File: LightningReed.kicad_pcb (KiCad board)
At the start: 0 parts

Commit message: Complete footprints
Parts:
- added C1: 470nF, LightningReed:C_Rect_L10.0mm_W6.0mm_P7.50mm_MKS4, F.Cu at (67.2, 63.9)
- added C10: 68uF, Capacitor_THT:CP_Radial_D18.0mm_P7.50mm, F.Cu at (25.8, 54.9)
- added C11: 1uF, Capacitor_SMD:C_0603_1608Metric, F.Cu at (21.2, 28.8)
- added C12: 1uF, Capacitor_SMD:C_0603_1608Metric, F.Cu at (21.2, 31.3)
- added C13: 1uF, Capacitor_SMD:C_0603_1608Metric, F.Cu at (21.2, 33.8)
- added C14: 220pF, Capacitor_SMD:C_0603_1608Metric, F.Cu at (21.2, 36.3)
- added C15: 1uF, Capacitor_SMD:C_0603_1608Metric, F.Cu at (21.2, 38.9)
- added C16: 100nF, Capacitor_SMD:C_0805_2012Metric, F.Cu at (84.6, 78.0)
- added C17: 220pF, Capacitor_SMD:C_0603_1608Metric, F.Cu at (21.2, 41.4)
- added C18: 100nF, Capacitor_SMD:C_1206_3216Metric, F.Cu at (55.9, 64.4)
- added C19: 470nF, Capacitor_SMD:C_1812_4532Metric, F.Cu at (39.6, 67.2)
- added C2: 220nF, LightningReed:C_Rect_L10.0mm_W6.0mm_P7.50mm_MKS4, F.Cu at (67.2, 71.5)
- added C20: 330nF, Capacitor_SMD:C_1210_3225Metric, F.Cu at (79.6, 62.3)
- added C21: 330nF, Capacitor_SMD:C_1210_3225Metric, F.Cu at (79.6, 66.5)
- added C22: 330nF, Capacitor_SMD:C_1210_3225Metric, F.Cu at (79.6, 70.8)
- added C23: 47nF, Capacitor_SMD:C_0603_1608Metric, F.Cu at (21.2, 43.9)
- added C24: 100nF, Capacitor_SMD:C_0603_1608Metric, F.Cu at (25.2, 16.3)
- added C25: 1uF, Capacitor_SMD:C_0603_1608Metric, F.Cu at (25.2, 18.8)
- added C26: 2.2uF, Capacitor_SMD:C_0603_1608Metric, F.Cu at (25.2, 21.3)
- added C27: 4.7uF, Capacitor_SMD:C_1210_3225Metric, F.Cu at (79.6, 75.0)
- added C28: 4.7uF, Capacitor_SMD:C_0805_2012Metric, F.Cu at (84.6, 81.0)
- added C29: 22uF, Capacitor_SMD:C_1210_3225Metric, F.Cu at (79.6, 79.3)
- added C30: 100nF, Capacitor_SMD:C_0603_1608Metric, F.Cu at (25.2, 23.8)
- added C31: 220pF, Capacitor_SMD:C_0603_1608Metric, F.Cu at (25.2, 26.3)
- added C32: 220pF, Capacitor_SMD:C_0603_1608Metric, F.Cu at (25.2, 28.8)
- added C33: 33pF, Capacitor_SMD:C_0603_1608Metric, F.Cu at (25.2, 31.3)
- added C34: 22pF, Capacitor_SMD:C_0603_1608Metric, F.Cu at (25.2, 33.8)
- added C35: 4.7nF, Capacitor_SMD:C_0603_1608Metric, F.Cu at (25.2, 36.3)
- added C36: 10nF, Capacitor_SMD:C_0603_1608Metric, F.Cu at (25.2, 38.9)
- added C37: 3.3pF, Capacitor_SMD:C_0603_1608Metric, F.Cu at (25.2, 41.4)
- added C38: 220pF, Capacitor_SMD:C_0603_1608Metric, F.Cu at (25.2, 43.9)
- added C39: 33uF, Capacitor_SMD:C_1206_3216Metric, F.Cu at (55.9, 67.7)
- added C4: 10pF, Capacitor_SMD:C_0805_2012Metric, F.Cu at (84.6, 75.0)
- added C40: 33uF, Capacitor_SMD:C_1206_3216Metric, F.Cu at (55.9, 71.1)
- added C41: 33uF, Capacitor_SMD:C_1206_3216Metric, F.Cu at (55.9, 74.4)
- added C42: 33uF, Capacitor_SMD:C_1206_3216Metric, F.Cu at (55.9, 77.8)
- added C43: 680uF, Capacitor_SMD:CP_Elec_10x10, F.Cu at (75.2, 38.3)
- added C44: 1uF, Capacitor_SMD:C_0603_1608Metric, F.Cu at (29.3, 16.3)
- added C45: 1uF, Capacitor_SMD:C_0603_1608Metric, F.Cu at (29.3, 18.8)
- added C46: 1uF, Capacitor_SMD:C_0603_1608Metric, F.Cu at (29.3, 21.3)
- added C47: 2.2uF, Capacitor_SMD:C_0603_1608Metric, F.Cu at (29.3, 23.8)
- added C5: 3900pF, Capacitor_SMD:C_0603_1608Metric, F.Cu at (21.2, 16.3)
- added C6: 1uF, Capacitor_SMD:C_0603_1608Metric, F.Cu at (21.2, 18.8)
- added C7: 33nF, Capacitor_SMD:C_0603_1608Metric, F.Cu at (21.2, 21.3)
- added C8: 220pF, Capacitor_SMD:C_0603_1608Metric, F.Cu at (21.2, 23.8)
- added C9: 2200pF, Capacitor_SMD:C_0603_1608Metric, F.Cu at (21.2, 26.3)
- added D1: ES3JF, Diode_SMD:D_SMF, F.Cu at (61.6, 64.4)
- added D10: SD103AW, Diode_SMD:D_SOD-123, F.Cu at (61.6, 71.1)
- added D11: BAS70WS, Diode_SMD:D_SOD-323, F.Cu at (45.4, 59.0)
- added D12: BZX84C16, Package_TO_SOT_SMD:SOT-23, F.Cu at (45.7, 34.6)
- added D13: MM3Z20, Diode_SMD:D_SOD-323, F.Cu at (45.4, 62.0)
- added D14: MM3Z24, Diode_SMD:D_SOD-323, F.Cu at (45.4, 64.9)
- added D15: RF081M2STR, Diode_SMD:D_SOD-123, F.Cu at (61.6, 74.4)
- added D16: MM3Z10, Diode_SMD:D_SOD-323, F.Cu at (45.4, 67.9)
- added D17: RFU02VSM8S, Diode_SMD:D_SOD-523, F.Cu at (80.5, 56.9)
- added D2: MSB40M, LightningReed:UMSB, F.Cu at (71.0, 79.2)
- added D3: ES2JW, Diode_SMD:D_SOD-123F, F.Cu at (84.7, 34.0)
- added D4: BZT52C16S, Diode_SMD:D_SOD-323, F.Cu at (45.4, 56.1)
- added D5: DSK16, Diode_SMD:D_SOD-123F, F.Cu at (84.7, 37.4)
- added D6: BZT52C13, Diode_SMD:D_SOD-123, F.Cu at (61.6, 67.7)
- added D7: STTH1R06A, Diode_SMD:D_SMA, F.Cu at (82.8, 48.9)
- added D8: ES1JW, Diode_SMD:D_SOD-123F, F.Cu at (84.7, 40.7)
- added D9: ES1JW, Diode_SMD:D_SOD-123F, F.Cu at (84.7, 44.1)
- added F1: JFC2410-1500TS, LightningReed:JFC2410, F.Cu at (82.8, 51.9)
- added L1: 5mH, LightningReed:CHOKE, F.Cu at (44.1, 15.8)
- added L2: 5mH, LightningReed:CHOKE, F.Cu at (44.1, 24.5)
- added L3: SDA0912-150uH-0.45, Inductor_THT:L_Radial_D12.0mm_P5.00mm_Fastron_11P, F.Cu at (69.5, 53.4)
- added L4: 7447709471, Inductor_SMD:L_12x12mm_H8mm, F.Cu at (60.5, 39.5)
- added L5: 1uH, LightningReed:CKST0603, F.Cu at (79.6, 19.1)
- added L6: 680nH, Inductor_SMD:L_0805_2012Metric, F.Cu at (38.3, 81.1)
- added P1: Conn_WallPlug, Connector_Wire:SolderWire-1sqmm_1x02_P5.4mm_D1.4mm_OD2.7mm, F.Cu at (62.5, 29.8)
- added Q1: NCE65T180D, Package_TO_SOT_SMD:TO-263-2, F.Cu at (68.7, 21.2)
- added Q10: DMZ6005E, Package_TO_SOT_SMD:SOT-23, F.Cu at (50.6, 39.0)
- added Q11: 2N7002K, Package_TO_SOT_SMD:SOT-23, F.Cu at (50.6, 43.5)
- added Q12: NCEP15T14D, Package_TO_SOT_SMD:LFPAK33, F.Cu at (38.8, 77.3)
- added Q13: BSS123, Package_TO_SOT_SMD:SOT-23, F.Cu at (50.6, 47.9)
- added Q2: 2N7002, Package_TO_SOT_SMD:SOT-23, F.Cu at (45.7, 39.0)
- added Q4: 2N7002, Package_TO_SOT_SMD:SOT-23, F.Cu at (45.7, 43.5)
- added Q5: 2N7002K, Package_TO_SOT_SMD:SOT-23, F.Cu at (45.7, 47.9)
- added Q6: 2N7002K, Package_TO_SOT_SMD:SOT-23, F.Cu at (45.7, 52.4)
- added Q7: NCE65T260K, Package_TO_SOT_SMD:TO-252-2, F.Cu at (59.1, 50.6)
- added Q8: NCE65T260K, Package_TO_SOT_SMD:TO-252-2, F.Cu at (59.1, 58.7)
- added Q9: NCE0102, Package_TO_SOT_SMD:SOT-23, F.Cu at (50.6, 34.6)
- added R1: 10, Resistor_SMD:R_0603_1608Metric, F.Cu at (29.3, 26.3)
- added R10: 3M24, Resistor_SMD:R_1206_3216Metric, F.Cu at (22.0, 82.8)
- added R11: 3M24, Resistor_SMD:R_1206_3216Metric, F.Cu at (27.6, 66.3)
- added R12: 3M24, Resistor_SMD:R_1206_3216Metric, F.Cu at (27.6, 69.6)
- added R13: 274K, Resistor_SMD:R_0603_1608Metric, F.Cu at (29.3, 36.3)
- added R14: 64k9, Resistor_SMD:R_0603_1608Metric, F.Cu at (29.3, 38.9)
- added R15: 2, Resistor_SMD:R_0603_1608Metric, F.Cu at (29.3, 41.4)
- added R16: 100K, Resistor_SMD:R_0603_1608Metric, F.Cu at (29.3, 43.9)
- added R17: 39K2, Resistor_SMD:R_0603_1608Metric, F.Cu at (33.3, 16.3)
- added R18: 100K, Resistor_SMD:R_0603_1608Metric, F.Cu at (33.3, 18.8)
- added R19: 3M24, Resistor_SMD:R_1206_3216Metric, F.Cu at (27.6, 72.9)
- added R2: 3M24, Resistor_SMD:R_1206_3216Metric, F.Cu at (22.0, 66.3)
- added R20: 3M24, Resistor_SMD:R_1206_3216Metric, F.Cu at (27.6, 76.2)
- added R21: 1K, Resistor_SMD:R_1206_3216Metric, F.Cu at (27.6, 79.5)
- added R22: 1K, Resistor_SMD:R_1206_3216Metric, F.Cu at (27.6, 82.8)
- added R23: 1K, Resistor_SMD:R_1206_3216Metric, F.Cu at (33.3, 66.3)
- added R24: 3M24, Resistor_SMD:R_1206_3216Metric, F.Cu at (33.3, 69.6)
- added R25: 3M16, Resistor_SMD:R_0805_2012Metric, F.Cu at (49.7, 56.1)
- added R26: 178K, Resistor_SMD:R_0603_1608Metric, F.Cu at (33.3, 21.3)
- added R27: 49K9, Resistor_SMD:R_0603_1608Metric, F.Cu at (33.3, 23.8)
- added R28: 100K, Resistor_SMD:R_0603_1608Metric, F.Cu at (33.3, 26.3)
- added R29: 10K, Resistor_SMD:R_0603_1608Metric, F.Cu at (33.3, 28.8)
- added R3: 3M24, Resistor_SMD:R_1206_3216Metric, F.Cu at (22.0, 69.6)
- added R30: 2M21, Resistor_SMD:R_1206_3216Metric, F.Cu at (33.3, 72.9)
- added R31: 10, Resistor_SMD:R_0603_1608Metric, F.Cu at (33.3, 31.3)
- added R32: 10K, Resistor_SMD:R_0603_1608Metric, F.Cu at (33.3, 33.8)
- added R33: 24.9, Resistor_SMD:R_0603_1608Metric, F.Cu at (33.3, 36.3)
- added R34: 10K, Resistor_SMD:R_0603_1608Metric, F.Cu at (33.3, 38.9)
- added R35: 10, Resistor_SMD:R_0603_1608Metric, F.Cu at (33.3, 41.4)
- added R36: 44K2, Resistor_SMD:R_0603_1608Metric, F.Cu at (33.3, 43.9)
- added R37: 118K, Resistor_SMD:R_0603_1608Metric, F.Cu at (37.3, 16.3)
- added R38: 220m, Resistor_SMD:R_1206_3216Metric, F.Cu at (33.3, 76.2)
- added R39: 220m, Resistor_SMD:R_1206_3216Metric, F.Cu at (33.3, 79.5)
- added R4: 3M24, Resistor_SMD:R_1206_3216Metric, F.Cu at (22.0, 72.9)
- added R40: 1, Resistor_SMD:R_0805_2012Metric, F.Cu at (49.7, 59.0)
- added R41: 1, Resistor_SMD:R_0805_2012Metric, F.Cu at (49.7, 62.0)
- added R42: 150K, Resistor_SMD:R_0603_1608Metric, F.Cu at (37.3, 18.8)
- added R43: 150K, Resistor_SMD:R_0603_1608Metric, F.Cu at (37.3, 21.3)
- added R44: 274K, Resistor_SMD:R_0603_1608Metric, F.Cu at (37.3, 23.8)
- added R45: 332K, Resistor_SMD:R_0603_1608Metric, F.Cu at (37.3, 26.3)
- added R46: 332K, Resistor_SMD:R_0603_1608Metric, F.Cu at (37.3, 28.8)
- added R47: 1K21, Resistor_SMD:R_0603_1608Metric, F.Cu at (37.3, 31.3)
- added R48: 1M, Resistor_SMD:R_0603_1608Metric, F.Cu at (37.3, 33.8)
- added R49: 121, Resistor_SMD:R_0603_1608Metric, F.Cu at (37.3, 36.3)
- added R5: 24K3, Resistor_SMD:R_0603_1608Metric, F.Cu at (29.3, 28.8)
- added R50: 12K4, Resistor_SMD:R_0603_1608Metric, F.Cu at (37.3, 38.9)
- added R51: 75K, Resistor_SMD:R_0603_1608Metric, F.Cu at (37.3, 41.4)
- added R52: 30K1, Resistor_SMD:R_0603_1608Metric, F.Cu at (37.3, 43.9)
- added R53: 432K, Resistor_SMD:R_0603_1608Metric, F.Cu at (41.3, 16.3)
- added R54: 10, Resistor_SMD:R_0603_1608Metric, F.Cu at (41.3, 18.8)
- added R55: 562, Resistor_SMD:R_0603_1608Metric, F.Cu at (41.3, 21.3)
- added R56: 10K, Resistor_SMD:R_0603_1608Metric, F.Cu at (41.3, 23.8)
- added R57: 15K, Resistor_SMD:R_0603_1608Metric, F.Cu at (41.3, 26.3)
- added R58: 150K, Resistor_SMD:R_0603_1608Metric, F.Cu at (41.3, 28.8)
- added R59: 56K2, Resistor_SMD:R_0603_1608Metric, F.Cu at (41.3, 31.3)
- added R6: 220m, Resistor_SMD:R_1206_3216Metric, F.Cu at (22.0, 76.2)
- added R60: 150K, Resistor_SMD:R_0603_1608Metric, F.Cu at (41.3, 33.8)
- added R61: 22, Resistor_SMD:R_0805_2012Metric, F.Cu at (49.7, 64.9)
- added R62: 100, Resistor_SMD:R_0603_1608Metric, F.Cu at (41.3, 36.3)
- added R63: 75K, Resistor_SMD:R_0603_1608Metric, F.Cu at (41.3, 38.9)
- added R7: 220m, Resistor_SMD:R_1206_3216Metric, F.Cu at (22.0, 79.5)
- added R8: 182K, Resistor_SMD:R_0603_1608Metric, F.Cu at (29.3, 31.3)
- added R9: 750, Resistor_SMD:R_0603_1608Metric, F.Cu at (29.3, 33.8)
- added TH1: 100K, Resistor_SMD:R_0603_1608Metric, F.Cu at (41.3, 41.4)
- added U1: UCC28056, Package_TO_SOT_SMD:SOT-23-6, F.Cu at (85.0, 62.4)
- added U2: 78L05S, Package_TO_SOT_SMD:SOT-89-3, F.Cu at (61.8, 79.1)
- added U3: LMC7111, Package_TO_SOT_SMD:SOT-23-5, F.Cu at (85.0, 66.8)
- added U4: UCC28780, Package_DFN_QFN:QFN-16-1EP_3x3mm_P0.5mm_EP1.45x1.45mm, F.Cu at (38.7, 72.3)
- added U5: UCC27712, Package_SO:SO-8_3.9x4.9mm_P1.27mm, F.Cu at (47.5, 72.6)
- added U6: LM317G, Package_TO_SOT_SMD:SOT-223-3_TabPin2, F.Cu at (82.4, 27.3)
- added U7: FODM8801A, Package_SO:SOP-4_4.4x2.6mm_P1.27mm, F.Cu at (48.1, 77.9)
- added U8: TL431DBZ, Package_TO_SOT_SMD:SOT-23, F.Cu at (50.6, 52.4)
- added U9: UCC24612-1DBV, Package_TO_SOT_SMD:SOT-23-5, F.Cu at (85.0, 71.3)
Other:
- copper layers 0 -> 2

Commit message: routing 1/?
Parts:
- added C3: 470nF, Capacitor_SMD:C_1812_4532Metric, F.Cu at (109.7, 134.9)
- added Q3: 1N60G, Package_TO_SOT_SMD:SOT-223-3_TabPin2, F.Cu at (35.3, 50.3)
- added T1: Transformer_2P_2S, LightningReed:RM10, F.Cu at (149.4, 126.0)
- added TP1: TestPoint_Alt, Connector_Wire:SolderWire-0.5sqmm_1x01_D0.9mm_OD2.1mm, F.Cu at (38.4, 64.8)
- added TP2: TestPoint_Alt, Connector_Wire:SolderWire-0.5sqmm_1x01_D0.9mm_OD2.1mm, F.Cu at (38.4, 68.9)
- added TP3: TestPoint_Alt, Connector_Wire:SolderWire-0.5sqmm_1x01_D0.9mm_OD2.1mm, F.Cu at (38.4, 73.1)
- added TP4: TestPoint_Alt, Connector_Wire:SolderWire-0.5sqmm_1x01_D0.9mm_OD2.1mm, F.Cu at (38.4, 77.2)
- D2, F1: moved to B.Cu
- Q12: footprint Package_TO_SOT_SMD:LFPAK33 -> Package_TO_SOT_SMD:TO-263-2
- moved L4 119.0 mm to (119.6, 142.7), turned to -90 degrees
- moved L2 110.0 mm to (100.5, 118.9)
- moved L1 105.0 mm to (100.3, 104.5)
- moved L3 96.5 mm to (103.9, 143.5)
- moved P1 83.5 mm to (104.2, 102.1)
- moved D1 81.2 mm to (94.1, 138.8)
- moved C19 77.5 mm to (102.4, 21.7)
- moved Q12 77.3 mm to (90.0, 19.5)
- moved C2 73.4 mm to (103.4, 135.3), turned to 90 degrees
- moved L5 66.6 mm to (42.7, 74.6)
- moved L6 64.4 mm to (102.6, 76.1)
- moved U4 64.2 mm to (103.0, 72.1)
- moved C1 61.8 mm to (101.7, 115.3)
- moved U1 61.4 mm to (101.4, 3.19)
- moved U3 61.4 mm to (101.4, 7.64)
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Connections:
- D12 pad 1: Net-(D12-K) -> GNDPWR
- D12 pad 2: GNDPWR -> (no net)
- D12 pad 3: (no net) -> Net-(D12-K)
- L2 pad 1: Net-(D2-Pad4) -> Net-(C1-Pad1)
- L2 pad 2: Net-(C1-Pad1) -> Net-(D2-Pad4)
- L2 pad 3: Net-(D2-Pad3) -> Net-(C1-Pad2)
- L2 pad 4: Net-(C1-Pad2) -> Net-(D2-Pad3)
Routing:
- net Net-(F1-Pad2): vias 0 -> 18
- net Net-(D2-Pad3): vias 0 -> 12
- net HT: vias 0 -> 12
- added copper zone on B.Cu, net GNDPWR
- added copper zone on F.Cu, net HT
- added copper zone on B.Cu, net Net-(C1-Pad1)
- added copper zone on B.Cu, net Net-(C1-Pad2)
- added copper zone on F.Cu, net Net-(D2-Pad3)
- added copper zone on B.Cu, net Net-(D2-Pad4)
- added copper zone on F.Cu, net Net-(F1-Pad2)
- added copper zone on F.Cu, net Net-(P1-AC_N)
- added copper zone on B.Cu, net Net-(P1-AC_P)
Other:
- board outline added: 50 x 50 mm

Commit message: PFC Layout
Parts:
- C11, C17, C4, C5, C6, C7, C8, D1, D3, D6, Q1, Q5, Q6, R1, R15, R2, R27, R28, R29, R3, R4, R5, R6, R7, R8, R9, U1: moved to B.Cu
- moved C6 180.9 mm to (141.5, 149.1), turned to 180 degrees
- moved C7 177.7 mm to (141.5, 147.6), turned to 180 degrees
- moved C5 171.7 mm to (132.8, 141.5), turned to 180 degrees
- moved C8 170.1 mm to (139.7, 141.7)
- moved C9 168.7 mm to (131.8, 148.6)
- moved R8 166.9 mm to (143.8, 148.3), turned to -90 degrees
- moved R29 164.6 mm to (148.1, 142.7)
- moved R28 164.0 mm to (144.0, 142.5)
- moved C17 163.3 mm to (146.3, 144.3)
- moved R27 162.6 mm to (146.6, 136.3), turned to 90 degrees
- moved C11 160.8 mm to (138.7, 135.4), turned to 90 degrees
- moved R5 158.8 mm to (134.1, 143.0)
- moved R9 157.5 mm to (136.7, 144.5), turned to -90 degrees
- moved R13 154.1 mm to (128.8, 148.6), turned to 180 degrees
- moved R1 152.9 mm to (128.5, 137.2)
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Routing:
- net /VCC_PFC: track 0.00 -> 9.27 mm, vias 0 -> 1
- net VDC: vias 0 -> 18
- net Net-(D3-A): vias 0 -> 30
- net Net-(D1-A): vias 0 -> 4
- net GNDPWR: vias 0 -> 12
- added copper zone on F.Cu, net Net-(D1-A)
- added copper zone on B.Cu, net Net-(D3-A)
- added copper zone on B.Cu, net VDC
- added copper zone on F.Cu, net VDC
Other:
- board size 50 x 50 mm -> 55 x 50 mm

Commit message: SR layout
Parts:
- added REF**: SolderWire-1sqmm_1x01_D1.4mm_OD2.7mm, Connector_Wire:SolderWire-1sqmm_1x01_D1.4mm_OD2.7mm, F.Cu at (127.3, 77.0)
- added TP10: TestPoint, Connector_Wire:SolderWire-0.15sqmm_1x01_D0.5mm_OD1.5mm, F.Cu at (130.6, 101.3)
- added TP11: TestPoint, Connector_Wire:SolderWire-0.15sqmm_1x01_D0.5mm_OD1.5mm, F.Cu at (130.6, 98.6)
- added TP12: TestPoint, Connector_Wire:SolderWire-0.15sqmm_1x01_D0.5mm_OD1.5mm, F.Cu at (127.3, 98.6)
- added TP13: TestPoint, Connector_Wire:SolderWire-0.15sqmm_1x01_D0.5mm_OD1.5mm, F.Cu at (144.3, 101.3)
- added TP14: TestPoint, Connector_Wire:SolderWire-0.15sqmm_1x01_D0.5mm_OD1.5mm, F.Cu at (147.6, 101.3)
- added TP15: TestPoint, Connector_Wire:SolderWire-0.15sqmm_1x01_D0.5mm_OD1.5mm, F.Cu at (144.3, 98.6)
- added TP16: TestPoint, Connector_Wire:SolderWire-0.15sqmm_1x01_D0.5mm_OD1.5mm, F.Cu at (147.6, 98.6)
- added TP5: TestPoint, Connector_Wire:SolderWire-1sqmm_1x01_D1.4mm_OD2.7mm, F.Cu at (140.0, 98.0)
- added TP6: TestPoint, Connector_Wire:SolderWire-1sqmm_1x01_D1.4mm_OD2.7mm, F.Cu at (140.0, 101.9)
- added TP7: TestPoint, Connector_Wire:SolderWire-1sqmm_1x01_D1.4mm_OD2.7mm, F.Cu at (134.6, 98.0)
- added TP8: TestPoint, Connector_Wire:SolderWire-1sqmm_1x01_D1.4mm_OD2.7mm, F.Cu at (134.6, 101.9)
- added TP9: TestPoint, Connector_Wire:SolderWire-0.15sqmm_1x01_D0.5mm_OD1.5mm, F.Cu at (127.3, 101.3)
- C36, C38, C39, C40, C41, C45, C47, D17, L5, L6, R59, R60, R61, R62, U7, U8, U9: moved to B.Cu
- TP1: footprint Connector_Wire:SolderWire-0.5sqmm_1x01_D0.9mm_OD2.1mm -> Connector_Wire:SolderWire-1sqmm_1x01_D1.4mm_OD2.7mm
- moved R24 106.1 mm to (74.9, 128.5)
- moved D4 100.7 mm to (88.7, 123.4)
- moved C36 100.6 mm to (152.1, 87.9)
- moved C35 98.4 mm to (145.5, 91.9), turned to 180 degrees
- moved C37 98.3 mm to (148.6, 91.9)
- moved R57 93.5 mm to (145.5, 93.5), turned to 180 degrees
- moved R56 92.0 mm to (144.8, 89.7), turned to 90 degrees
- moved R58 91.8 mm to (148.6, 90.4), turned to 180 degrees
- moved R59 88.9 mm to (149.1, 87.9), turned to 180 degrees
- moved R60 88.9 mm to (152.1, 86.4)
- moved R20 88.9 mm to (74.9, 115.3)
- moved R22 88.9 mm to (74.9, 121.9)
- moved R23 88.9 mm to (74.9, 125.2)
- moved R19 88.9 mm to (74.9, 112.0)
- moved R21 88.9 mm to (74.9, 118.6)
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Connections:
- T1 pad 10: VS -> Net-(T1-SD-Pad10)
- T1 pad 13: GNDS -> Net-(T1-SB)
- T1 pad 8: /VAUX -> Net-(T1-SC-Pad8)
- T1 pad 9: Net-(Q12-S) -> Net-(T1-SA)
- U7 pad 3: GNDPWR -> Net-(TP16-Pad1)
- U7 pad 4: Net-(R52-Pad1) -> Net-(TP15-Pad1)
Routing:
- net GNDPWR: track 0.00 -> 42.8 mm, vias 12 -> 37
- net VS: track 0.00 -> 32.3 mm, vias 0 -> 1
- net LINE: track 0.00 -> 27.3 mm, vias 0 -> 28
- net Net-(Q12-S): track 0.00 -> 25.8 mm, vias 0 -> 1
- net VCOM: track 0.00 -> 24.2 mm, vias 0 -> 47
- net GNDS: track 0.00 -> 22.1 mm, vias 0 -> 135
- net Net-(T1-SC-Pad8): track 0.00 -> 20.3 mm
- net Net-(D3-A): track 0.00 -> 19.5 mm
- net Net-(U1-DRV): track 0.00 -> 18.0 mm
- net /COMP: track 0.00 -> 16.0 mm, vias 0 -> 2
- net Net-(Q5-G): track 0.00 -> 15.9 mm
- net Net-(U8-K): track 0.00 -> 15.7 mm, vias 0 -> 1
- net Net-(U1-VCC): track 0.00 -> 15.5 mm, vias 0 -> 2
- net /CTL: track 0.00 -> 14.0 mm, vias 0 -> 1
- net Net-(T1-SA): track 0.00 -> 13.9 mm
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- added copper zone on F.Cu, net GNDPWR
- added copper zone on B.Cu, net GNDS
- added copper zone on F.Cu, net GNDS
- added copper zone on F.Cu, net LINE
- added copper zone on B.Cu, net Net-(Q1-S)
- added copper zone on F.Cu, net Net-(Q1-S)
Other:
- board size 55 x 50 mm -> 55 x 75 mm

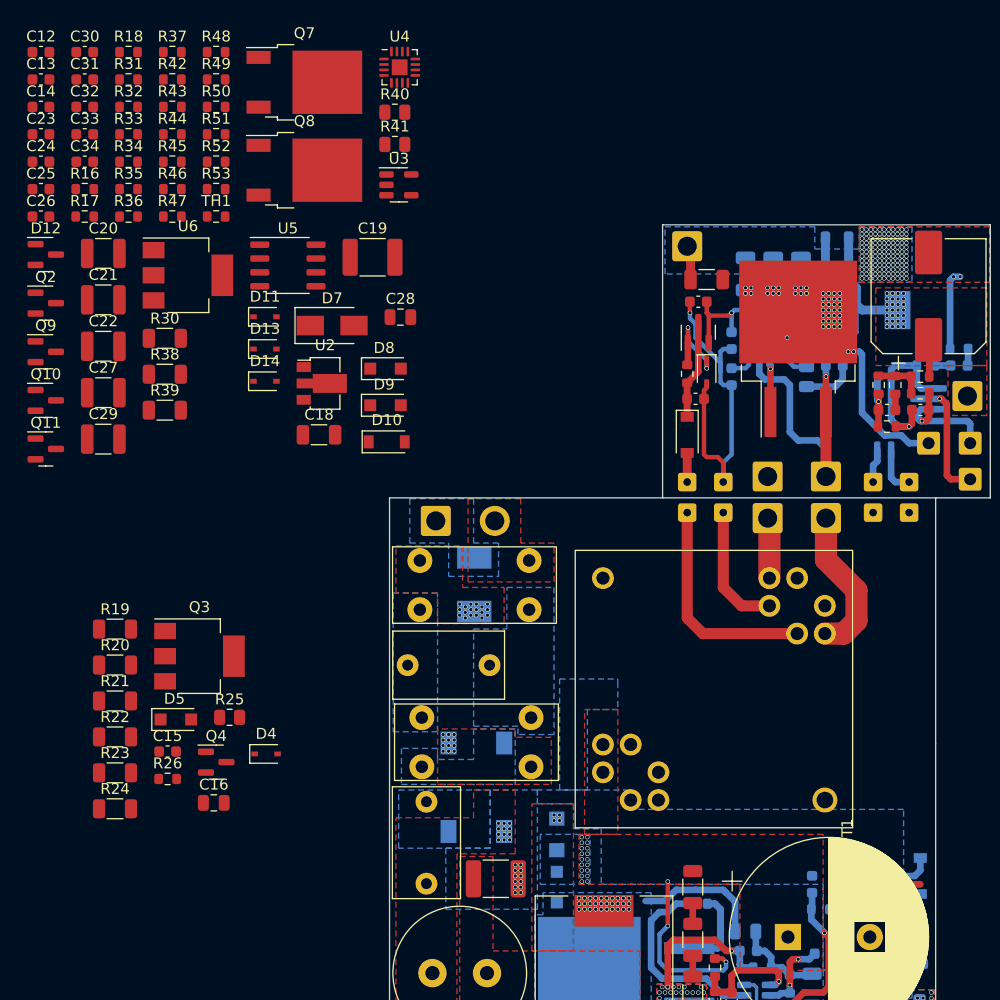
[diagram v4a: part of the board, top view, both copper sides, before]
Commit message: Flyback controller left - layout
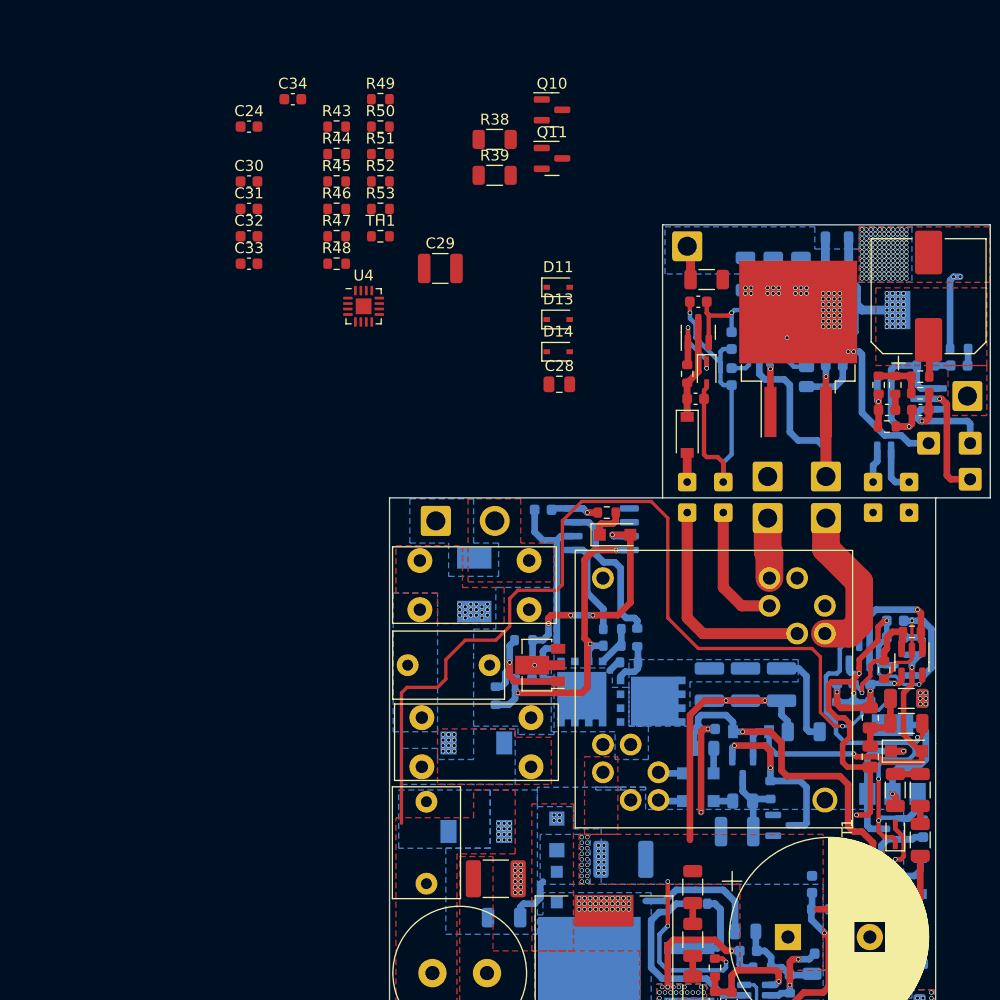
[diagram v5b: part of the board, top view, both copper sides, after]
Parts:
- C12, C13, C14, C15, C18, C19, C20, C21, C22, C23, C25, C26, C27, D10, D12, D8, D9, Q2, Q3, Q4, Q9, R17, R19, R26, R30, R31, R32, R33, R34, R40, R41, R42, U5: moved to B.Cu
- D7: value STTH1R06A -> U1J; footprint Diode_SMD:D_SMA -> Diode_SMD:D_SOD-123F
- Q7, Q8: value NCE65T260K -> CMSA65R280Q; footprint Package_TO_SOT_SMD:TO-252-2 -> Package_SON:VSONP-8-1EP_5x6_P1.27mm; moved to B.Cu
- R36: value 44K2 -> 470; moved to B.Cu
- R37: value 118K -> 3K24; moved to B.Cu
- U2: footprint Package_TO_SOT_SMD:SOT-89-3 -> Package_TO_SOT_SMD:SOT-23; moved to B.Cu
- U6: value LM317G -> LM317LCPK; footprint Package_TO_SOT_SMD:SOT-223-3_TabPin2 -> Package_TO_SOT_SMD:SOT-89-3
- moved C12 94.8 mm to (146.3, 112.8), turned to 180 degrees
- moved C14 93.0 mm to (144.0, 117.9), turned to -90 degrees
- moved C13 92.6 mm to (146.3, 111.3), turned to 180 degrees
- moved R18 89.2 mm to (147.8, 112.3), turned to 180 degrees
- moved R16 85.4 mm to (145.3, 115.8), turned to -90 degrees
- moved D12 85.4 mm to (136.1, 130.0)
- moved R42 85.0 mm to (134.9, 126.7), turned to -90 degrees
- moved R17 82.8 mm to (142.5, 117.9), turned to 90 degrees
- moved Q2 81.1 mm to (143.0, 114.2), turned to 90 degrees
- moved C26 76.9 mm to (129.0, 121.2), turned to 180 degrees
- moved R21 74.8 mm to (148.6, 131.3), turned to 90 degrees
- moved Q9 74.3 mm to (132.3, 124.7), turned to -90 degrees
- moved R22 73.9 mm to (148.6, 126.7), turned to 90 degrees
- moved R24 72.9 mm to (147.3, 120.7), turned to 180 degrees
- moved R19 72.7 mm to (147.3, 118.4), turned to 180 degrees
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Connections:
- C28 pad 2: Net-(D11-K) -> VDD
- C29 pad 2: Net-(D11-K) -> VDD
- D11 pad 1: Net-(D11-K) -> VDD
- Q7 pad 1: Net-(Q7-G) -> /VSW
- Q7 pad 2: Net-(Q7-D) -> Net-(Q7-G)
- Q7 pad 3: /VSW -> Net-(Q7-D)
- Q8 pad 1: Net-(Q8-G) -> Net-(Q8-S)
- Q8 pad 2: /VSW -> Net-(Q8-G)
- Q8 pad 3: Net-(Q8-S) -> /VSW
- T1 pad 1: /VSW -> GNDPWR
- T1 pad 2: (no net) -> Net-(D9-A)
- T1 pad 5: Net-(D9-A) -> /VSV
- T1 pad 6: GNDPWR -> (no net)
- T1 pad 7: /VSV -> /VSW
- U4 pad 15: Net-(D11-K) -> VDD
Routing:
- net HT: track 0.00 -> 88.0 mm, vias 12 -> 13
- net GNDPWR: track 42.8 -> 100.6 mm, vias 37 -> 45
- net VDC: track 0.00 -> 47.0 mm, vias 18 -> 32
- net /BROWN_OUT: track 0.00 -> 43.3 mm, vias 0 -> 3
- net /VDD3: track 0.00 -> 35.2 mm, vias 0 -> 2
- net /VDD2: track 4.11 -> 38.3 mm, vias 0 -> 2
- net Net-(Q8-S): track 0.00 -> 30.5 mm, vias 0 -> 3
- net Net-(D7-A): track 0.00 -> 24.9 mm, vias 0 -> 5
- net /VSW: track 0.00 -> 21.8 mm
- net /5V_LDO: track 0.00 -> 15.6 mm, vias 0 -> 1
- net Net-(D12-K): track 0.00 -> 15.5 mm, vias 0 -> 2
- net Net-(U5-HO): track 0.00 -> 14.0 mm
- net Net-(Q2-G): track 0.00 -> 12.8 mm, vias 0 -> 1
- net Net-(Q3-D): track 0.00 -> 12.5 mm, vias 0 -> 1
- net Net-(D5-K): track 0.00 -> 12.5 mm, vias 0 -> 1
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- added copper zone on B.Cu, net /VSW
- added copper zone on B.Cu, net Net-(Q7-D)

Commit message: Controller 50%
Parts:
- C24, C30, C31, R38, R39, R43, R44, R45, R47, U4: moved to B.Cu
- moved C34 98.0 mm to (161.7, 131.5)
- moved R49 95.2 mm to (165.7, 131.5)
- moved R50 95.2 mm to (165.7, 134.0)
- moved C32 90.0 mm to (161.7, 126.5)
- moved C33 90.0 mm to (161.7, 129.0)
- moved R51 86.7 mm to (169.7, 119.0)
- moved TH1 86.7 mm to (169.7, 126.5)
- moved R48 86.7 mm to (165.7, 129.0)
- moved R52 86.7 mm to (169.7, 121.5)
- moved R53 86.7 mm to (169.7, 124.0)
- moved R46 84.2 mm to (161.8, 125.0)
- moved Q10 81.2 mm to (174.2, 119.9)
- moved Q11 81.2 mm to (174.2, 124.4)
- moved D11 74.1 mm to (178.8, 119.2)
- moved D13 74.1 mm to (178.8, 122.1)
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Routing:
- net Net-(Q8-S): track 30.5 -> 71.8 mm, vias 3 -> 21
- net GNDPWR: track 100.6 -> 139.9 mm, vias 45 -> 48
- net VDD: track 0.00 -> 25.8 mm, vias 0 -> 4
- net /BUR: track 0.00 -> 12.4 mm, vias 0 -> 2
- net /VREF: track 0.00 -> 9.78 mm
- net /PWML: track 0.00 -> 8.87 mm, vias 0 -> 2
- net /PWMH: track 0.00 -> 8.55 mm
- net Net-(U4-RTZ): track 0.00 -> 4.61 mm
- net /FB: track 0.00 -> 4.21 mm
- net /CS: track 0.00 -> 4.05 mm
- net Net-(U4-RDM): track 0.00 -> 2.51 mm
- net Net-(T1-SC-Pad8): track 20.3 -> 17.9 mm
- net HT: track 88.0 -> 88.7 mm
- net Net-(T1-SD-Pad10): track 11.8 -> 11.1 mm
- added copper zone on B.Cu, net Net-(Q8-S)
- added copper zone on F.Cu, net Net-(Q8-S)
